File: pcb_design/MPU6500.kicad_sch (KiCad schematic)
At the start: 9 parts, among them U5 MPU-6500

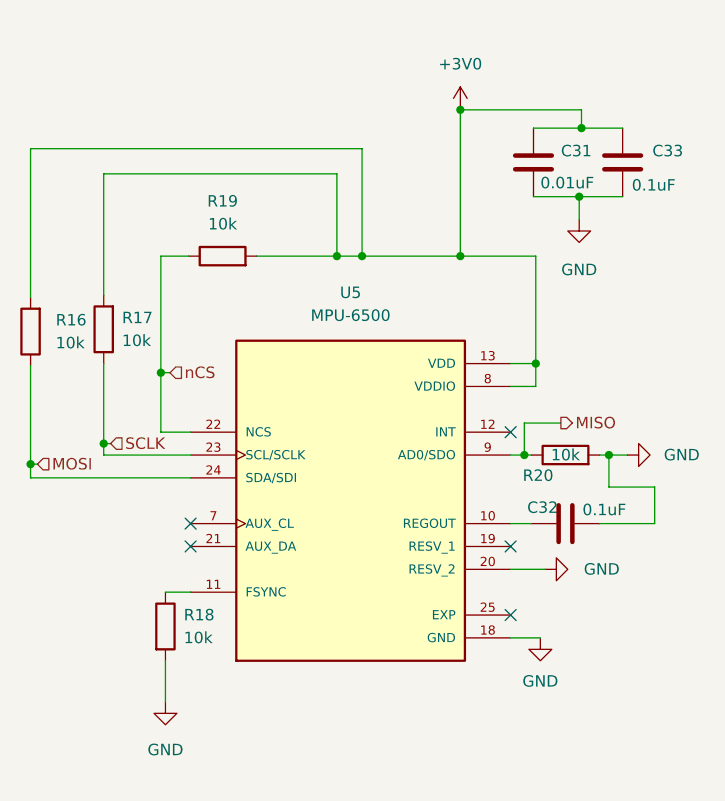
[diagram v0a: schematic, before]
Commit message: Update Mushak PCB design to include new features (#5)
* Update mushak PCB with new changes
* Add AMS1117 as 3.3v regulator
* Add new alternate placement for IR sensors
* Add new 3.3v compatible ToF sensor
* Update gerber files

* Add changes to silkscreen and filter capacitors
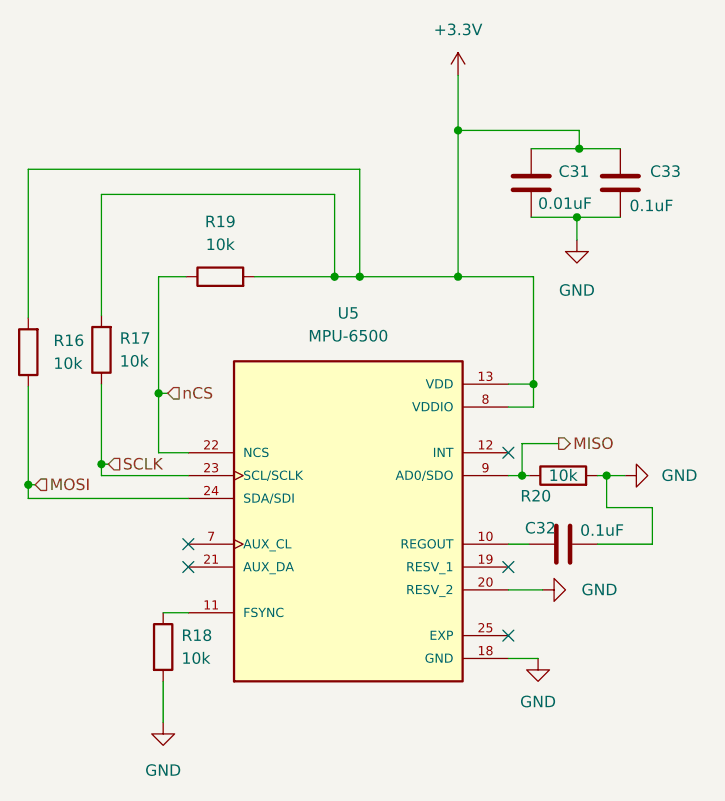
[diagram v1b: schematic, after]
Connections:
- net +3V0 renamed +3.3V
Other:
- moved on the sheet: C31, C32, C33, R16, R17, R18, R19, R20, U5
